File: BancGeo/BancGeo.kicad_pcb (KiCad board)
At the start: 2 copper layers, 127.5 x 96.5 mm, 126 parts, among them P1 Alim, P10 GND, P2 Batt, P3 CONN_01X05, P4 Capt1, P5 Capt2, P6 Capt3, P7 Capt4, P8 USB_D-, P9 USB_D+, Q1 2N7002E, Q2 PMV37EN2R, Q3 PMV37EN2R, Q4 2N7002E, Q5 2N7002E, Q6 2N7002E, SW1 SWITCH_BRIDE, SW2 SW_PUSH, T1 DRQ127-100-R, U1 MCP9700A, U10 MCP1754T-3302E/OT, U11 HM-10_BLE_Module, U12 LM4120IM5X-5.0/NOPB, U2 TC54VC4302ECB713, U3 MCP6546, U4 LM4120IM5X-5.0/NOPB, U5 MCP1754T-5002E/OT, U6 MCP1631X-ML_QFN, U7 PIC16F18323_QFN, U8 ADS1115, U9 MCP23008-QFN_PCKG

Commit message: update BancGeo
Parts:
- moved R43 4.50 mm to (162.3, 132.9)
- moved D9 3.85 mm to (99.1, 142.7)
- moved C27 3.54 mm to (95.2, 144.7), turned to 270 degrees
- moved D8 2.85 mm to (163.8, 142.7)
- moved T1 0.75 mm to (173.2, 138.2)
- moved C16 0.75 mm to (173.2, 128.9)
- moved C12 0.75 mm to (173.3, 147.0)
- moved C15 0.75 mm to (173.3, 148.9)
- moved R18 0.60 mm to (180.2, 141.1)
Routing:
- net GND: track 704.9 -> 723.5 mm, vias 86 -> 93
- net /SetPreChg: track 112.4 -> 119.4 mm
- net /SetTail: track 108.8 -> 115.7 mm
- net Net-(D8-Pad2): track 4.54 -> 11.2 mm, vias 0 -> 2
- net Net-(R43-Pad2): track 37.3 -> 32.8 mm
- net Net-(D9-Pad2): track 4.04 -> 7.93 mm, vias 0 -> 1
- net /+5V: track 438.1 -> 440.5 mm
- net /Tx_µC: track 26.1 -> 27.4 mm
- net /Rx_µC: track 27.6 -> 28.7 mm

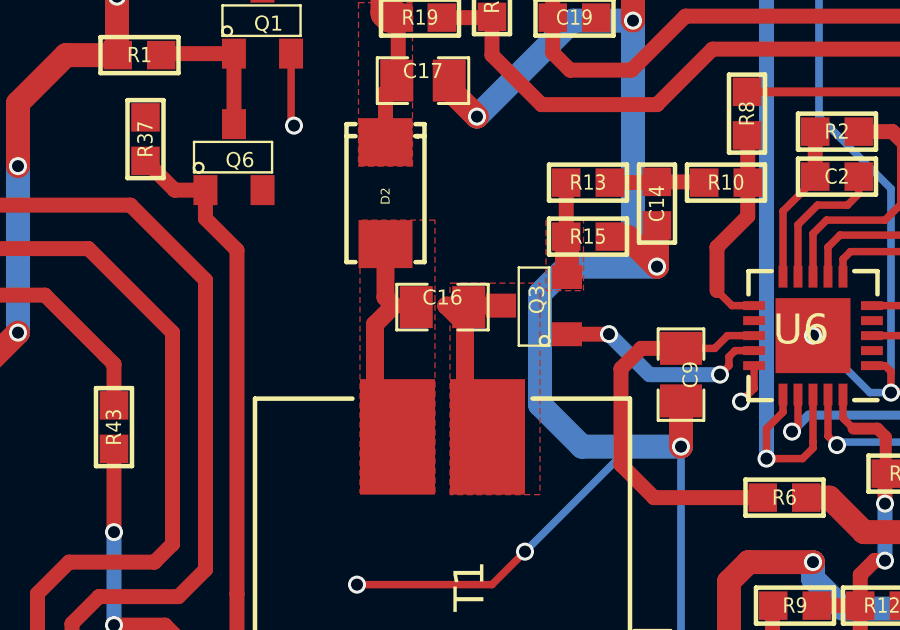
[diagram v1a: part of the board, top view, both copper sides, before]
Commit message: Update IACSENSE and send to fab BancGeo & IACSense
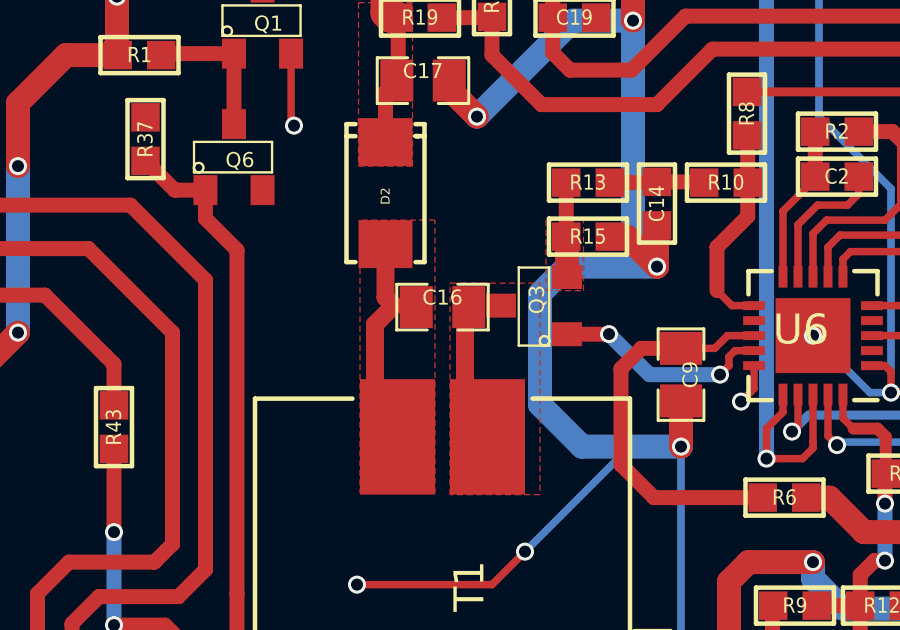
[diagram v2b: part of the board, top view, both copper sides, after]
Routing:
- net /TR_High_Side: track 6.41 -> 4.92 mm
- net /Self_Out_2: track 6.75 -> 7.52 mm
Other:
- rule pad_to_mask_clearance: 0.07 -> 0.1
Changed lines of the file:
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@@
     (thickness 1.6)
     (drawings 20)
-    (tracks 1514)
+    (tracks 1517)
     (zones 0)
     (modules 126)
@@
   )
   (setup
-    (last_trace_width 0.5)
+    (last_trace_width 0.25)
     (user_trace_width 0.25)
     (user_trace_width 0.3)
@@
     (pad_size 1.9 1.9)
     (pad_drill 1)
-    (pad_to_mask_clearance 0.07)
+    (pad_to_mask_clearance 0.1)
+    (solder_mask_min_width 0.1)
     (aux_axis_origin 0 0)
     (grid_origin 191.05 100.75)
     (visible_elements FFFFFF3F)
     (pcbplotparams
-      (layerselection 0x00020_00000000)
-      (usegerberextensions false)
-      (excludeedgelayer false)
+      (layerselection 0x010c0_80000001)
+      (usegerberextensions true)
+      (excludeedgelayer true)
       (linewidth 0.100000)
       (plotframeref false)
@@
       (padsonsilk false)
       (subtractmaskfromsilk false)
-      (outputformat 5)
+      (outputformat 1)
       (mirror false)
       (drillshape 0)
       (scaleselection 1)
-      (outputdirectory Gerber))
+      (outputdirectory ./Gerber))
   )
   (net 0 "")
@@
     (effects (font (size 1.5 1.5) (thickness 0.3)))
   )
-  (gr_text GP7 (at 104.5 139.7) (layer F.Mask)
+  (gr_text GP7 (at 98.65 140.05) (layer F.Mask)
     (effects (font (size 1.5 1.5) (thickness 0.3)))
   )
@@
   (segment (start 177.39982 127.9475) (end 177.39982 126.62482) (width 0.8) (layer F.Cu) (net 80))
   (segment (start 177.39982 126.62482) (end 177.375 126.6) (width 0.8) (layer F.Cu) (net 80))
+  (segment (start 174.125 128.95) (end 174.125 129.4) (width 0.25) (layer F.Cu) (net 81))
+  (segment (start 174.125 129.4) (end 174 129.525) (width 0.25) (layer F.Cu) (net 81))
+  (segment (start 174 129.525) (end 174.125 128.95) (width 0.25) (layer F.Cu) (net 81))
   (segment (start 174 133.225) (end 174 129.525) (width 0.6) (layer F.Cu) (net 81))
-  (segment (start 174 129.525) (end 173.375 128.9) (width 0.6) (layer F.Cu) (net 81))
-  (segment (start 175.20018 128.9) (end 173.375 128.9) (width 0.6) (layer F.Cu) (net 81))
   (segment (start 179.65 141.725) (end 178.675 141.725) (width 0.8) (layer F.Cu) (net 82))
   (segment (start 177.225 143.175) (end 174 143.175) (width 0.8) (layer F.Cu) (net 82))
@@
   (segment (start 186.85 127.1) (end 190.1 127.1) (width 0.25) (layer F.Cu) (net 82))
   (segment (start 186.6 127.35) (end 186.85 127.1) (width 0.25) (layer F.Cu) (net 82))
+  (segment (start 171.625 128.9) (end 172.325 128.9) (width 0.25) (layer F.Cu) (net 83))
+  (segment (start 172.325 128.9) (end 172.375 128.95) (width 0.25) (layer F.Cu) (net 83))
   (segment (start 171.35 126.85) (end 171.35 128.625) (width 0.6) (layer F.Cu) (net 83))
   (segment (start 171.35 128.625) (end 171.625 128.9) (width 0.6) (layer F.Cu) (net 83))

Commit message: Update layout
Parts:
- removed U11: HM-10_BLE_Module, Yame_library:HM-10_BLE
- removed U9: MCP23008-QFN_PCKG, Housings_DFN_QFN:QFN-20-1EP_4x4mm_Pitch0.5mm
- C22: value 100n -> 1u
- R10, R13: value R -> 1k
- R19: value R -> 270k
- R20: value R -> 100k
- R21: value R -> 47k
- R3: value 750k -> 220k
- R4: value 220k -> 100k
- R7: value 10k -> 100
- R8: value R -> 20k
- U10: value MCP1754T-3302E/OT -> MCP1754ST-3302E/CB
- U5: value MCP1754T-5002E/OT -> MCP1754ST-5002E/CB
- U6: value MCP1631X-ML_QFN -> MCP1631V-ML_QFN
- moved U2 3.99 mm to (183.2, 104.7)
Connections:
- net Net-(P3-Pad1) renamed /ICSPDATA
- net Net-(P3-Pad2) renamed /ICSPCLK
- net Net-(P3-Pad4) renamed //MCLR
- C7 pad 1: /+Vbat -> Net-(C7-Pad1)
- P2 pad 2: Net-(P2-Pad2) -> GND
- Q2 pad 3: Net-(P2-Pad2) -> Net-(Q2-Pad3)
- R3 pad 1: /+Vref1 -> /+5V
- R9 pad 2: /+Vref2 -> /+5V
- U5 pad 3: /+Vbat -> Net-(C7-Pad1)
- U7 pad 10: /Vtemp -> /SCL
- U7 pad 2: /Vsense -> /SDA
- U7 pad 8: /SDA -> /Vsense
- U7 pad 9: /SCL -> /Vtemp
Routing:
- net /+Vbat: track 198.5 -> 189.9 mm
- net /Vtemp: track 41.1 -> 36.8 mm
- net /+Vref2: track 145.9 -> 142.0 mm
- net Net-(P2-Pad2): track 2.61 -> 0.28 mm
- net /Vsense: track 7.48 -> 6.16 mm
- net /SCL: track 59.3 -> 58.5 mm
- net /+Vref1: track 94.9 -> 94.2 mm
- net /SDA: track 58.5 -> 58.0 mm
- net GND: vias 93 -> 94
